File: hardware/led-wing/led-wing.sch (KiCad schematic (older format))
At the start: 48 parts, among them J1 Feather, SW1 SW_Push, SW2 SW_Push, SW3 SW_Push, SW4 SW_Push, U1 CD74HC4050

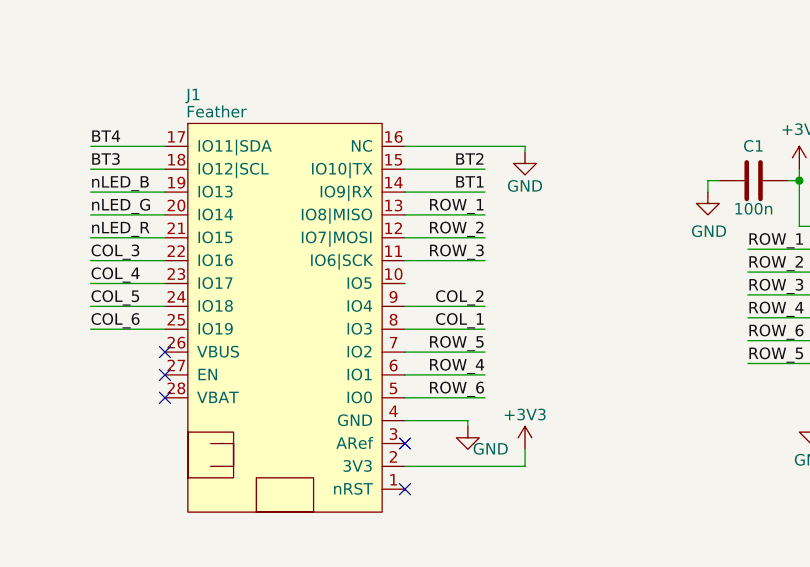
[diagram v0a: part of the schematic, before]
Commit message: generated gerbers, changed pin labelling to match constraints file
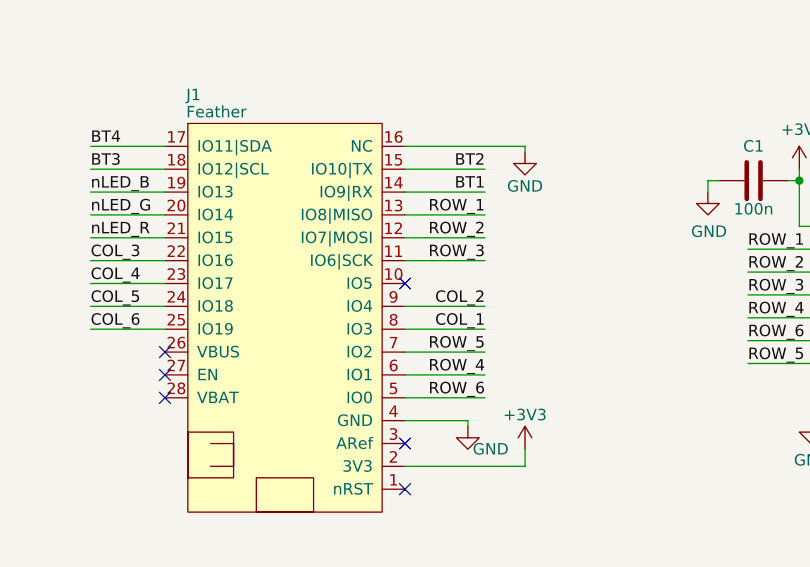
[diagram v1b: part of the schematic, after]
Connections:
- no-connect marks 5 -> 6
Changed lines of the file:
@@
 Text Label 10275 4700 1    50   ~ 0
 C2
+NoConn ~ 5250 3025
 $EndSCHEMATC
